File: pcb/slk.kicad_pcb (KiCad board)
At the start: 2 copper layers, 68.6 x 53.3 mm, 15 parts, among them J1 Screw Terminal, P1 Power, P2 Analog, P3 Digital 1, P4 Digital 2, U1 MCP2515-xSO, U2 TJA1055T1, Y1 Crystal

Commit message: it should work now
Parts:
- moved U2 35.2 mm to (153.7, 67.2)
- moved C1 14.8 mm to (130.3, 81.3), turned to -90 degrees
- moved C2 14.7 mm to (135.9, 81.3), turned to -90 degrees
- moved Y1 10.8 mm to (133.1, 76.2)
- moved R1 8.57 mm to (126.5, 58.4)
- moved U1 7.96 mm to (132.0, 66.0)
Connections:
- P3 pad 4: unconnected-(P3-Pin_4-Pad4) -> /INH
- P3 pad 5: unconnected-(P3-Pin_5-Pad5) -> /ERR
- P3 pad 6: unconnected-(P3-Pin_6-Pad6) -> /STB
- P3 pad 7: unconnected-(P3-Pin_7-Pad7) -> /EN
- P3 pad 8: unconnected-(P3-Pin_8-Pad8) -> /WAKE
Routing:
- net /GND: track 13.1 -> 129.9 mm
- net /CANH: track 1.40 -> 57.0 mm
- net /BAT+: track 0.97 -> 56.5 mm
- net /CANL: track 2.04 -> 56.1 mm
- net /5V: track 46.8 -> 94.7 mm
- net /RX: track 6.53 -> 37.3 mm
- net /TX: track 10.4 -> 32.9 mm
- net /WAKE: track 0.00 -> 12.5 mm
- net /ERR: track 0.00 -> 12.0 mm
- net /EN: track 0.00 -> 12.0 mm
- net /STB: track 0.00 -> 11.4 mm
- net /INH: track 0.00 -> 11.4 mm
- net Net-(U1-OSC1): track 18.6 -> 10.1 mm
- net Net-(U1-OSC2): track 17.5 -> 11.9 mm
- net Net-(U1-~{RESET}): track 7.18 -> 3.46 mm
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
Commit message: leds
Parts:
- added D1: ERR, LED_SMD:LED_0603_1608Metric, F.Cu at (161.8, 61.0)
- added D2: RX, LED_SMD:LED_0603_1608Metric, F.Cu at (143.0, 64.8)
- added D3: TX, LED_SMD:LED_0603_1608Metric, F.Cu at (143.0, 68.6)
- added R1: R, Resistor_SMD:R_0402_1005Metric, F.Cu at (165.6, 61.0)
- added R2: R, Resistor_SMD:R_0402_1005Metric, F.Cu at (146.8, 64.8)
- added R3: R, Resistor_SMD:R_0402_1005Metric, F.Cu at (146.6, 68.6)
- added SW1: SW_SPDT, Button_Switch_SMD:SW_SPDT_CK_JS102011SAQN, F.Cu at (109.6, 92.7)
- Y1: value Crystal -> 16MHz
- moved J1 14.0 mm to (106.7, 67.3), turned to -90 degrees
- renumbered R1 to R4
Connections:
- J1 pad 1: /BAT+ -> /CANH
- J1 pad 3: /CANH -> /BAT+
- U2 pad 14: /BAT+ -> Net-(SW1-B)
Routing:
- net Net-(SW1-B): track 0.00 -> 56.8 mm
- net /GND: track 129.9 -> 73.3 mm, vias 0 -> 5
- net /BAT+: track 56.5 -> 12.0 mm
- net /5V: track 94.7 -> 129.3 mm, vias 0 -> 4
- net /ERR: track 12.0 -> 26.0 mm
- net /CANH: track 57.0 -> 61.2 mm
- net Net-(D1-A): track 0.00 -> 2.54 mm
- net Net-(D2-A): track 0.00 -> 2.49 mm
- net /CANL: track 56.1 -> 58.5 mm
- net Net-(D3-A): track 0.00 -> 2.24 mm
- net /TX: track 32.9 -> 34.3 mm
- net /RX: track 37.3 -> 38.5 mm
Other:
- board text added: "5V"
- board text added: "BAT"
- board text added: "BATTERY +"
- board text added: "CAN HIGH"
- board text added: "CAN LOW"
- board text added: "ERR"
- board text added: "RX"
- board text added: "TX"
- board text added: "slkworld.com rulez!"

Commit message: done
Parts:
- R1, R2, R3: value R -> 330

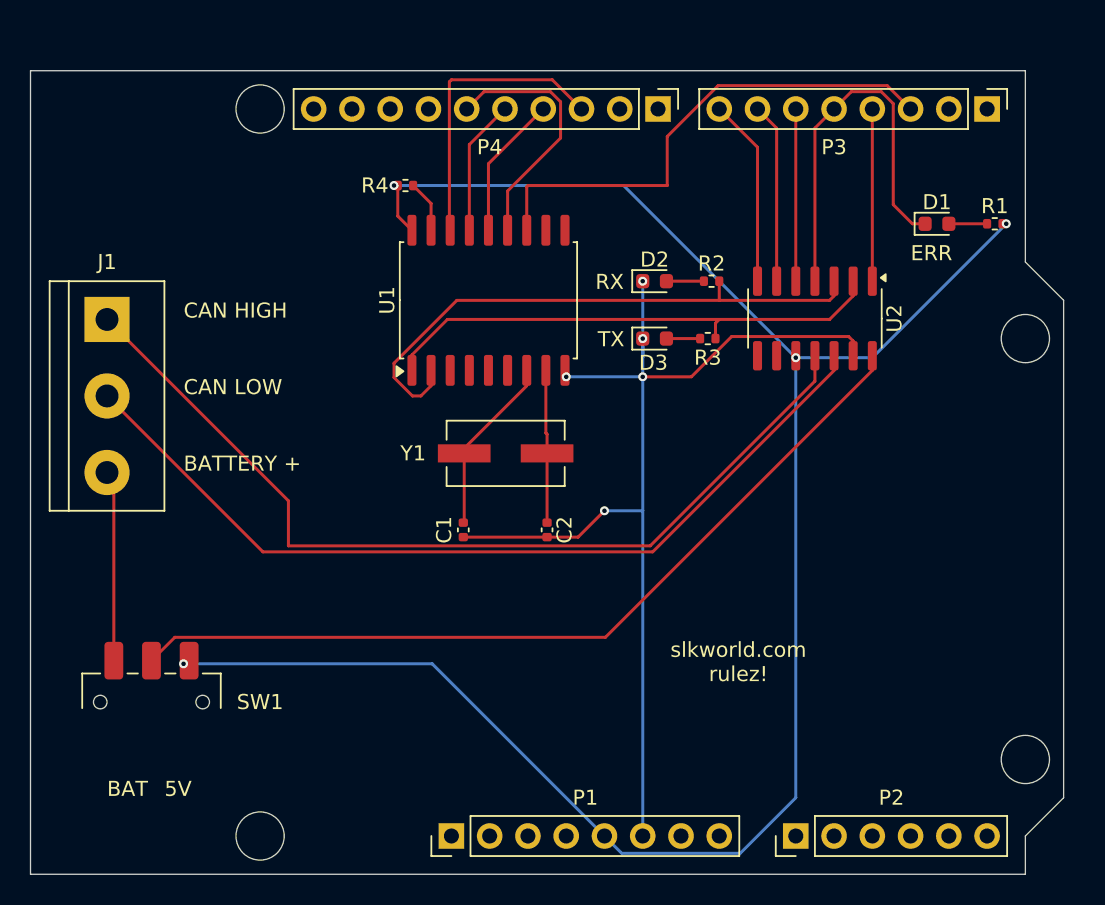
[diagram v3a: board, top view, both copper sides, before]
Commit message: add manual resistors
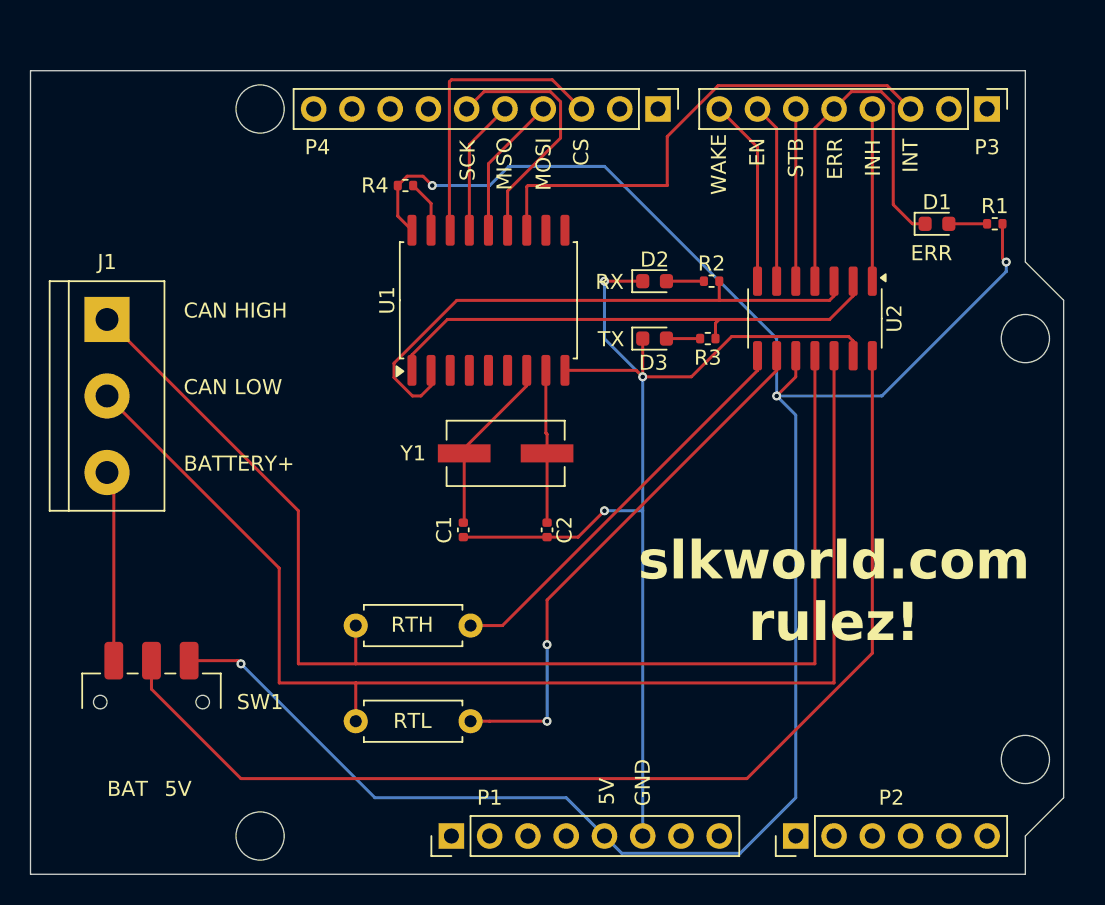
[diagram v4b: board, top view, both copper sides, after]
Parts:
- added R5: R, Resistor_THT:R_Axial_DIN0207_L6.3mm_D2.5mm_P7.62mm_Horizontal, F.Cu at (130.8, 94.0)
- added R6: R, Resistor_THT:R_Axial_DIN0207_L6.3mm_D2.5mm_P7.62mm_Horizontal, F.Cu at (130.8, 87.6)
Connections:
- net Net-(SW1-B) renamed /BAT
- U2 pad 8: unconnected-(U2-RTH-Pad8) -> /RTH
- U2 pad 9: unconnected-(U2-RTL-Pad9) -> /RTL
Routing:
- net /RTL: track 0.00 -> 35.7 mm, vias 0 -> 2
- net /RTH: track 0.00 -> 27.0 mm
- net /CANL: track 58.5 -> 84.9 mm
- net /CANH: track 61.2 -> 85.4 mm
- net /BAT: track 56.8 -> 75.4 mm
- net /5V: track 129.3 -> 137.5 mm
- net /GND: track 73.3 -> 77.1 mm, vias 5 -> 3
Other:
- board text added: "BATTERY+"
- board text added: "CS"
- board text added: "EN"
- board text added: "GND"
- board text added: "INH"
- board text added: "INT"
- board text added: "MISO"
- board text added: "MOSI"
- board text added: "RTH"
- board text added: "RTL"
- board text added: "SCK"
- board text added: "STB"
- board text added: "WAKE"
- board text removed: "BATTERY +"
